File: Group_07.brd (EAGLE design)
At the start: 100 x 80 mm, 29 parts, among them J1 POWER_JACKPTH_LOCK, U1 +12v, U3 TCA9546ASO16, U4 TMUX1208

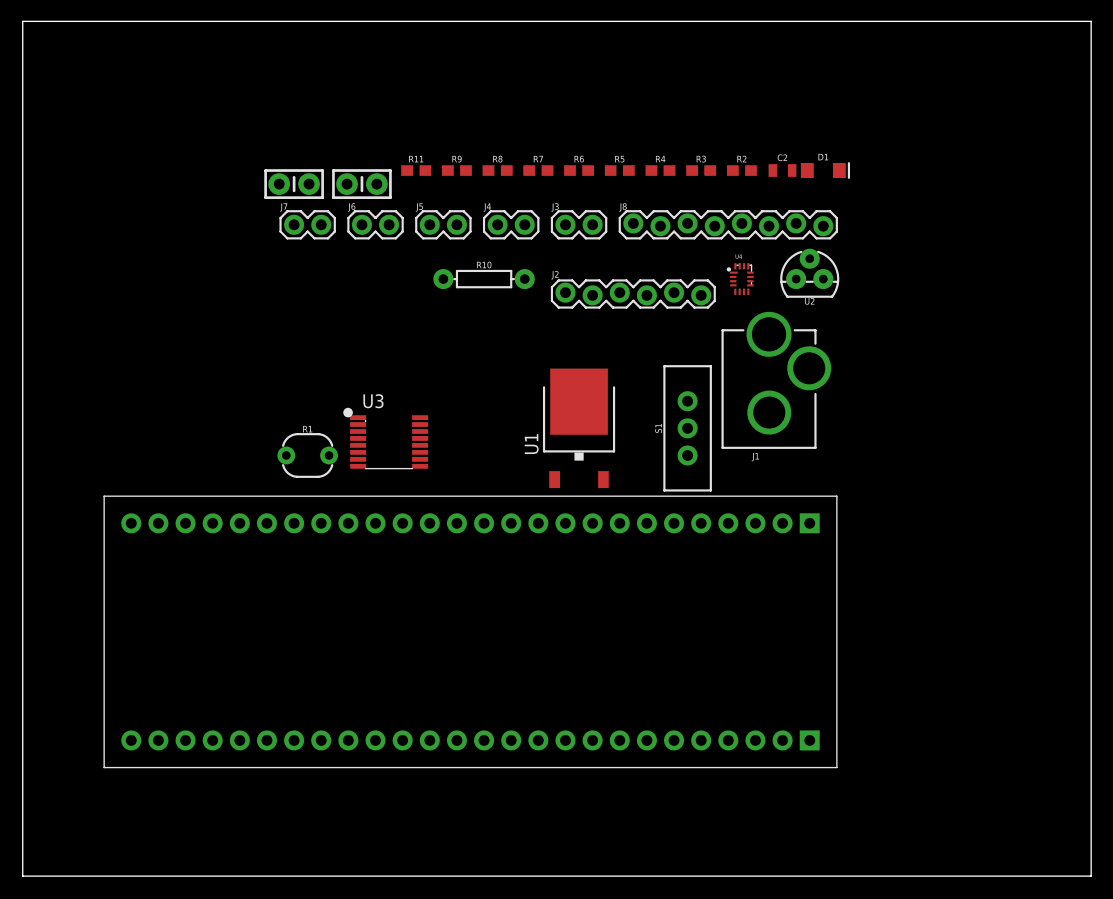
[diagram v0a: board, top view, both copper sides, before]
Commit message: Disposition of the components and traces
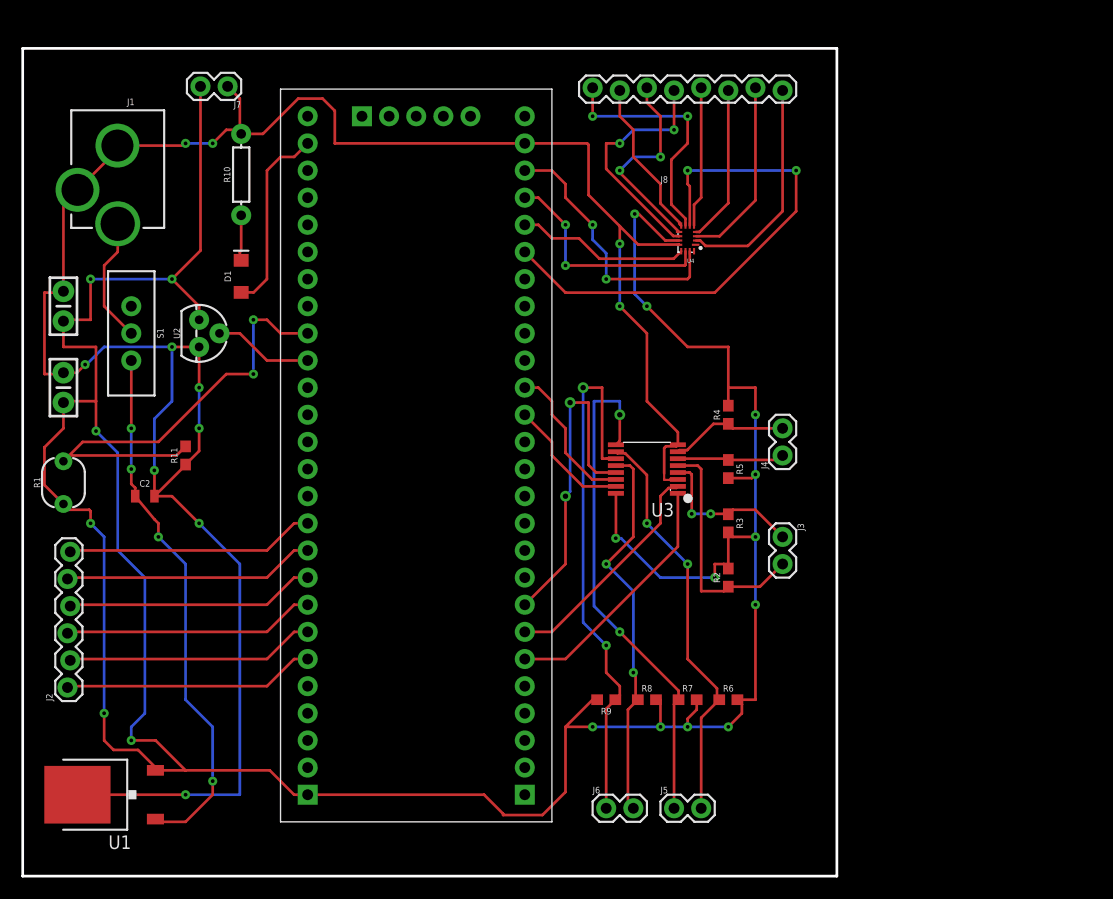
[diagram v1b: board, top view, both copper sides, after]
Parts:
- removed U$4: CY8CKIT-059_TARGET_3, CY8KIT-059:CY8CKIT-059_TARGET_3
- added U$1: CY8CKIT-059_TARGET, CYKIT:CY8CKIT-059_TARGET
- moved J1 71.9 mm to (8.89, 74.9), turned to 180 degrees
- moved C2 67.0 mm to (11.4, 35.6)
- moved J2 59.5 mm to (4.19, 17.7), turned to 90 degrees
- moved J5 59.2 mm to (61.0, 6.35)
- moved J6 59.2 mm to (54.6, 6.35)
- moved U2 57.4 mm to (16.5, 50.8), turned to 270 degrees
- moved U1 56.1 mm to (7.62, 7.62), turned to 90 degrees
- moved D1 55.4 mm to (20.4, 56.1), turned to 90 degrees
- moved S1 52.8 mm to (10.2, 50.8), turned to 180 degrees
- moved R6 51.5 mm to (66.0, 16.5)
- moved R7 51.5 mm to (62.2, 16.5)
- moved R8 51.5 mm to (58.4, 16.5)
- moved R9 51.5 mm to (54.6, 16.5), turned to 180 degrees
- moved R2 38.1 mm to (66.0, 27.9), turned to 90 degrees
- moved J3 35.6 mm to (71.1, 31.8), turned to 270 degrees
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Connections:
- removed net GND2: U$4.52
- net 5V: now also U$1.27; no longer U$4.27
- net GND: now also U$1.25; no longer U$4.25
- net I2C_A0: now also U$1.6; no longer U$4.6
- net I2C_A1: now also U$1.7; no longer U$4.7
- net I2C_A2: now also U$1.8; no longer U$4.8
- net I2C_SCL: now also U$1.16; no longer U$4.16
- net I2C_SDA: now also U$1.15; no longer U$4.15
- net MUX_A0/1.3C: now also U$1.24; no longer U$4.24
- net MUX_A1/1.4C: now also U$1.23; no longer U$4.23
- net MUX_A2/1.4C: now also U$1.22; no longer U$4.22
- net MUX_OUT/1.4C: now also U$1.21; no longer U$4.21
- net N$18: now also U$1.26; no longer U$4.26
- net N$20: now also U$1.28; no longer U$4.28
- net N$3: now also U$1.37; no longer U$4.37
- net N$4: now also U$1.36; no longer U$4.36
- net N$5: now also U$1.35; no longer U$4.35
- net N$6: now also U$1.34; no longer U$4.34
- net N$7: now also U$1.33; no longer U$4.33
- net N$8: now also U$1.32; no longer U$4.32
- net N$9: now also U$1.51; no longer U$4.51
- net PHOTO_OUT: now also U$1.44; no longer U$4.44
- net TEMP_OUT: now also U$1.43; no longer U$4.43
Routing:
- net 5V: track 0.00 -> 298.5 mm, vias 0 -> 18
- net GND: track 0.00 -> 216.8 mm, vias 0 -> 11
- net I2C_SDA_3: track 0.00 -> 51.9 mm, vias 0 -> 2
- net 12V: track 0.00 -> 50.2 mm, vias 0 -> 4
- net MUX_OUT/1.4C: track 0.00 -> 49.3 mm, vias 0 -> 2
- net I2C_SDA_2: track 0.00 -> 48.2 mm, vias 0 -> 2
- net PHOTO_OUT: track 0.00 -> 43.9 mm, vias 0 -> 2
- net I2C_SCL_2: track 0.00 -> 38.6 mm, vias 0 -> 2
- net I2C_SCL_3: track 0.00 -> 37.1 mm, vias 0 -> 2
- net I2C_A2: track 0.00 -> 31.1 mm, vias 0 -> 2
- net MUX_A0/1.3C: track 0.00 -> 25.1 mm, vias 0 -> 2
- net I2C_A0: track 0.00 -> 23.7 mm
- net N$8: track 0.00 -> 23.6 mm
- net N$4: track 0.00 -> 23.6 mm
- net N$6: track 0.00 -> 23.6 mm
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- added copper zone on layer 16, net 5V
- added copper zone on layer 1, net GND
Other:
- board size 100 x 80 mm -> 76.2 x 77.5 mm

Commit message: modifica delle dimensioni vias
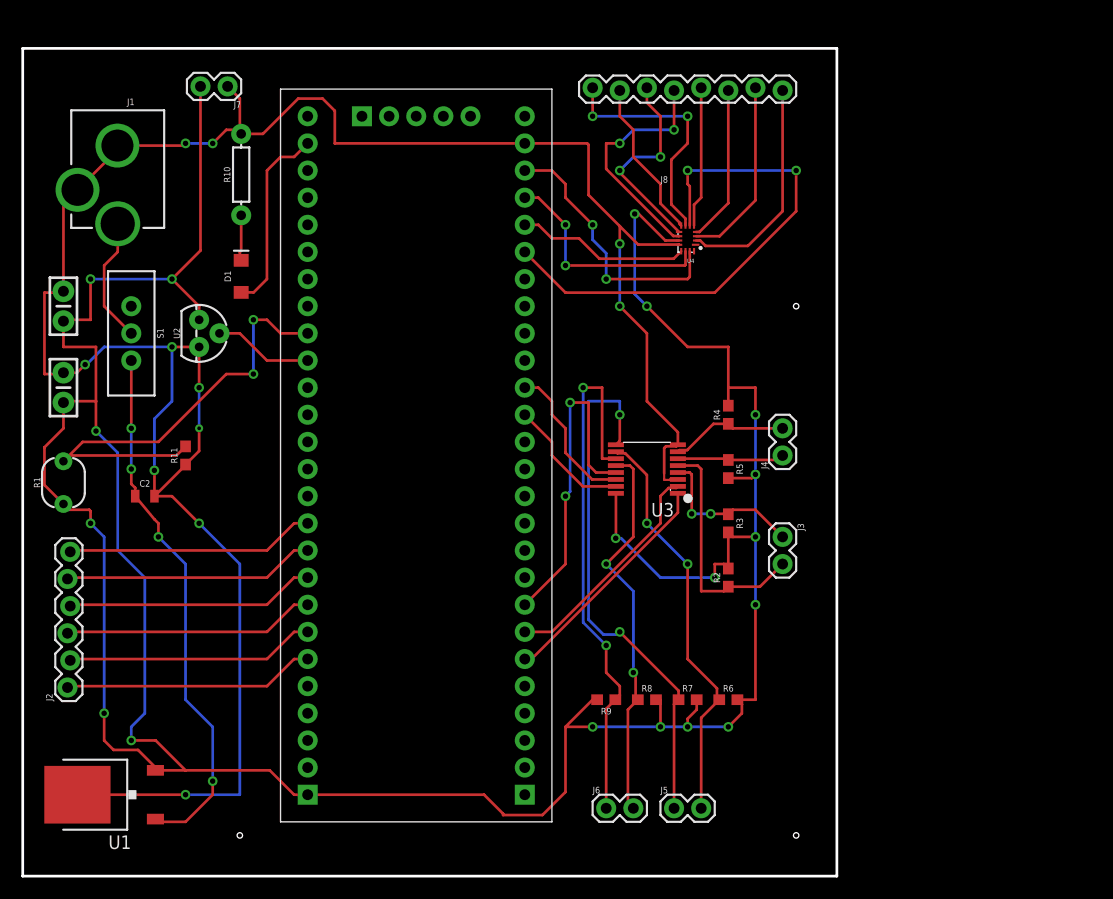
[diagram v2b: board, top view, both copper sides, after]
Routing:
- net I2C_SDA_2: track 48.2 -> 50.2 mm
- net I2C_A0: track 23.7 -> 21.8 mm
- net I2C_SDA_3: track 51.9 -> 51.0 mm

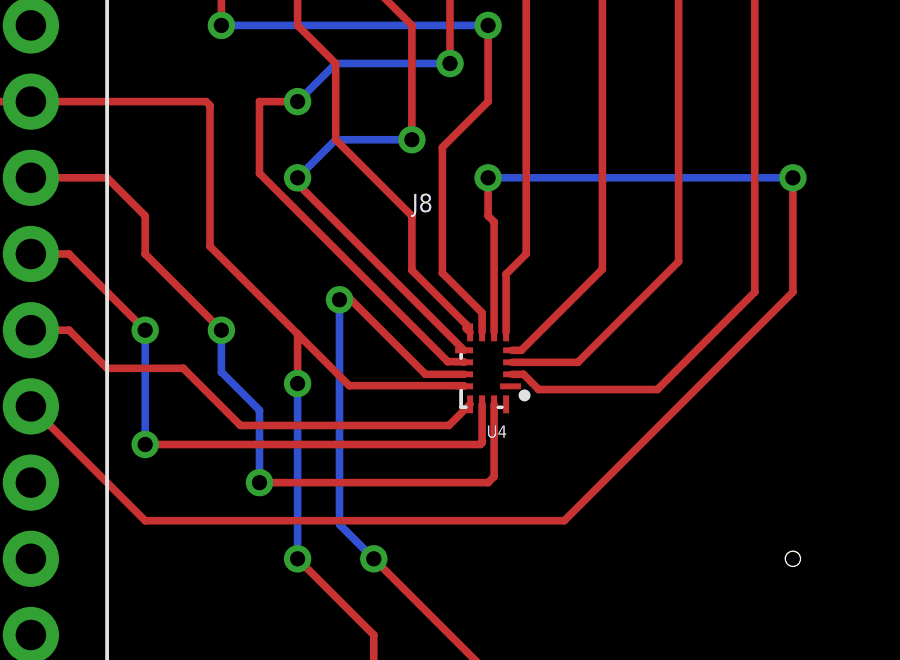
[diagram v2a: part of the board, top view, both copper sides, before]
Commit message: airwire da fixare per problemi di clearance
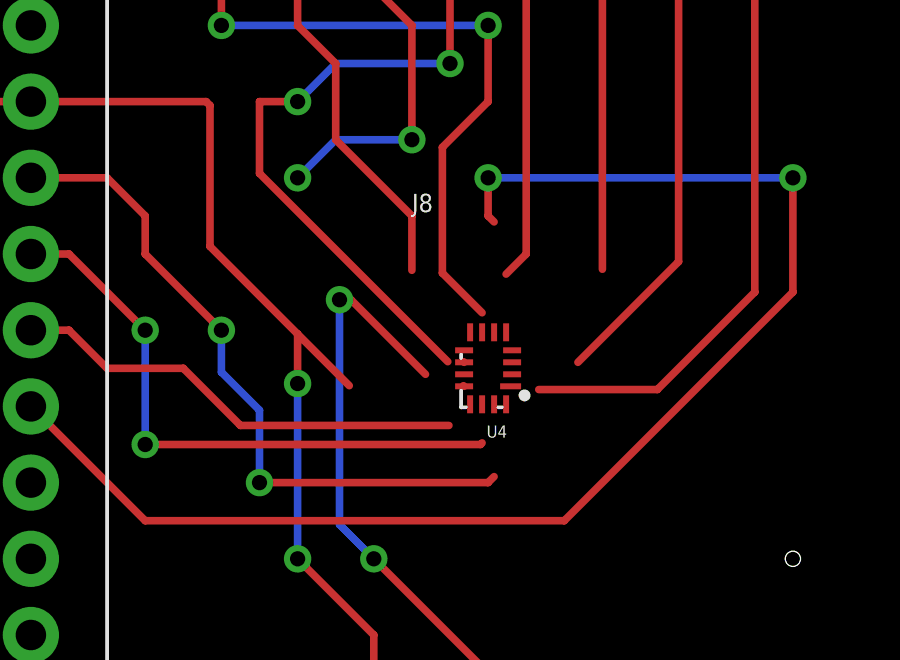
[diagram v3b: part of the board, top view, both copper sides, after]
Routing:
- net N$15: track 19.4 -> 11.5 mm
- net N$12: track 14.7 -> 10.5 mm
- net GND: track 216.7 -> 212.9 mm
- net MUX_OUT/1.4C: track 49.3 -> 45.7 mm
- net N$16: track 15.0 -> 12.2 mm
- net MUX_A0/1.3C: track 25.1 -> 22.7 mm
- net N$11: track 17.5 -> 15.3 mm
- net N$13: track 13.2 -> 11.2 mm
- net MUX_A1/1.4C: track 21.2 -> 19.9 mm
- net 5V: track 298.5 -> 297.2 mm
- net N$2: track 20.9 -> 19.8 mm
- net MUX_A2/1.4C: track 16.2 -> 15.3 mm
- net N$17: track 23.0 -> 22.3 mm
- net N$14: track 22.4 -> 21.9 mm
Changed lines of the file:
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@@
 <wire x1="2.032" y1="40.132" x2="2.032" y2="36.608" width="0.254" layer="1"/>
 <wire x1="2.032" y1="36.608" x2="3.81" y2="34.83" width="0.254" layer="1"/>
-<wire x1="61.43" y1="59.49" x2="60.144" y2="59.49" width="0.254" layer="1"/>
 <wire x1="57.658" y1="61.976" x2="57.277" y2="61.976" width="0.254" layer="1"/>
 <via x="57.277" y="61.976" extent="1-16" drill="0.508"/>
@@
 <wire x1="7.62" y1="31.75" x2="7.62" y2="15.24" width="0.254" layer="16"/>
 <wire x1="8.509" y1="11.811" x2="10.789" y2="11.811" width="0.254" layer="1"/>
+<wire x1="60.144" y1="59.49" x2="61.43" y2="59.49" width="0" layer="19" extent="1-1"/>
 </signal>
 <signal name="N$1">
@@
 </polygon>
 <wire x1="61.43" y1="59.09" x2="61.4094" y2="59.1106" width="0.254" layer="1"/>
-<wire x1="61.4094" y1="59.1106" x2="57.6024" y2="59.1106" width="0.254" layer="1"/>
 <wire x1="57.6024" y1="59.1106" x2="55.88" y2="60.833" width="0.254" layer="1"/>
 <wire x1="55.88" y1="60.833" x2="52.959" y2="63.754" width="0.254" layer="1"/>
@@
 <wire x1="60.071" y1="37.084" x2="60.5552" y2="37.084" width="0.2032" layer="1"/>
 <wire x1="60.5552" y1="37.084" x2="60.5962" y2="37.125" width="0.2032" layer="1"/>
+<wire x1="57.6024" y1="59.1106" x2="61.4094" y2="59.1106" width="0" layer="19" extent="1-1"/>
 </signal>
 <signal name="12V">
@@
 <contactref element="U$1" pad="24"/>
 <contactref element="U4" pad="15"/>
-<wire x1="62.43" y1="58.49" x2="62.43" y2="56.08" width="0.254" layer="1"/>
 <wire x1="62.43" y1="56.08" x2="62.23" y2="55.88" width="0.254" layer="1"/>
 <wire x1="62.23" y1="55.88" x2="54.61" y2="55.88" width="0.254" layer="1"/>
@@
 <wire x1="50.8" y1="64.77" x2="49.53" y2="66.04" width="0.254" layer="1"/>
 <wire x1="49.53" y1="66.04" x2="46.99" y2="66.04" width="0.254" layer="1"/>
+<wire x1="62.43" y1="56.08" x2="62.43" y2="58.49" width="0" layer="19" extent="1-1"/>
 </signal>
 <signal name="MUX_A1/1.4C">
 <contactref element="U$1" pad="23"/>
 <contactref element="U4" pad="14"/>
-<wire x1="62.03" y1="58.49" x2="62.03" y2="57.204" width="0.254" layer="1"/>
 <wire x1="62.03" y1="57.204" x2="61.976" y2="57.15" width="0.254" layer="1"/>
 <wire x1="61.976" y1="57.15" x2="50.8" y2="57.15" width="0.254" layer="1"/>
@@
 <wire x1="50.8" y1="60.96" x2="48.26" y2="63.5" width="0.254" layer="1"/>
 <wire x1="48.26" y1="63.5" x2="46.99" y2="63.5" width="0.254" layer="1"/>
+<wire x1="62.03" y1="57.204" x2="62.03" y2="58.49" width="0" layer="19" extent="1-1"/>
 </signal>
 <signal name="MUX_A2/1.4C">
@@
 <wire x1="52.07" y1="59.69" x2="53.975" y2="57.785" width="0.254" layer="1"/>
 <wire x1="53.975" y1="57.785" x2="60.925" y2="57.785" width="0.254" layer="1"/>
-<wire x1="60.925" y1="57.785" x2="61.63" y2="58.49" width="0.254" layer="1"/>
+<wire x1="60.925" y1="57.785" x2="61.63" y2="58.49" width="0" layer="19" extent="1-1"/>
 </signal>
 <signal name="MUX_OUT/1.4C">
 <contactref element="U$1" pad="21"/>
 <contactref element="U4" pad="6"/>
-<wire x1="62.43" y1="60.89" x2="62.43" y2="64.57" width="0.254" layer="1"/>
 <wire x1="62.43" y1="64.57" x2="62.23" y2="64.77" width="0.254" layer="1"/>
 <wire x1="62.23" y1="64.77" x2="62.23" y2="66.04" width="0.254" layer="1"/>
@@
 <wire x1="64.77" y1="54.61" x2="50.8" y2="54.61" width="0.254" layer="1"/>
 <wire x1="50.8" y1="54.61" x2="46.99" y2="58.42" width="0.254" layer="1"/>
+<wire x1="62.43" y1="64.57" x2="62.43" y2="60.89" width="0" layer="19" extent="1-1"/>
 </signal>
 <signal name="N$2">
@@
 <contactref element="U4" pad="2"/>
 <wire x1="67.872" y1="58.982" x2="63.919" y2="58.982" width="0.254" layer="1"/>
-<wire x1="63.919" y1="58.982" x2="63.411" y2="59.49" width="0.254" layer="1"/>
-<wire x1="63.03" y1="59.49" x2="63.411" y2="59.49" width="0.254" layer="1"/>
 <wire x1="67.872" y1="58.982" x2="71.12" y2="62.23" width="0.254" layer="1"/>
 <wire x1="71.12" y1="62.23" x2="71.12" y2="73.533" width="0.254" layer="1"/>
+<wire x1="63.03" y1="59.49" x2="63.919" y2="58.982" width="0" layer="19" extent="1-1"/>
 </signal>
 <signal name="N$11">
 <contactref element="J8" pad="7"/>
 <contactref element="U4" pad="3"/>
-<wire x1="63.03" y1="59.89" x2="65.224" y2="59.89" width="0.254" layer="1"/>
 <wire x1="65.224" y1="59.89" x2="68.58" y2="63.246" width="0.254" layer="1"/>
 <wire x1="68.58" y1="63.246" x2="68.58" y2="73.787" width="0.254" layer="1"/>
+<wire x1="63.03" y1="59.89" x2="65.224" y2="59.89" width="0" layer="19" extent="1-1"/>
 </signal>
 <signal name="N$12">
 <contactref element="J8" pad="6"/>
 <contactref element="U4" pad="4"/>
-<wire x1="63.03" y1="60.29" x2="63.338" y2="60.29" width="0.254" layer="1"/>
 <wire x1="66.04" y1="62.992" x2="66.04" y2="73.533" width="0.254" layer="1"/>
-<wire x1="63.338" y1="60.29" x2="66.04" y2="62.992" width="0.254" layer="1"/>
+<wire x1="63.03" y1="60.29" x2="66.04" y2="62.992" width="0" layer="19" extent="1-1"/>
 </signal>
 <signal name="N$13">
 <contactref element="J8" pad="5"/>
 <contactref element="U4" pad="5"/>
-<wire x1="62.83" y1="60.89" x2="62.83" y2="62.83" width="0.254" layer="1"/>
-<wire x1="62.83" y1="62.83" x2="63.5" y2="63.5" width="0.254" layer="1"/>
+<wire x1="63.5" y1="63.5" x2="62.83" y2="62.83" width="0.254" layer="1"/>
 <wire x1="63.5" y1="63.5" x2="63.5" y2="73.787" width="0.254" layer="1"/>
+<wire x1="62.83" y1="62.83" x2="62.83" y2="60.89" width="0" layer="19" extent="1-1"/>
 </signal>
 <signal name="N$14">
@@
 <contactref element="U4" pad="10"/>
 <wire x1="61.43" y1="59.89" x2="61.4094" y2="59.9106" width="0.254" layer="1"/>
-<wire x1="61.4094" y1="59.9106" x2="60.88726875" y2="59.9106" width="0.254" layer="1"/>
 <wire x1="60.88726875" y1="59.9106" x2="54.61" y2="66.18786875" width="0.254" layer="1"/>
 <wire x1="54.61" y1="66.18786875" x2="54.61" y2="68.58" width="0.254" layer="1"/>
@@
 <wire x1="60.96" y1="69.85" x2="60.96" y2="73.533" width="0.254" layer="1"/>
 <wire x1="57.15" y1="69.85" x2="60.96" y2="69.85" width="0.254" layer="16"/>
+<wire x1="60.88726875" y1="59.9106" x2="61.4094" y2="59.9106" width="0" layer="19" extent="1-1"/>
 </signal>
 <signal name="N$15">
@@
 <wire x1="59.69" y1="71.12" x2="58.42" y2="72.39" width="0.254" layer="1"/>
 <wire x1="58.42" y1="72.39" x2="58.42" y2="73.787" width="0.254" layer="1"/>
-<wire x1="61.43" y1="60.29" x2="55.88" y2="65.84" width="0.254" layer="1"/>
 <wire x1="55.88" y1="65.84" x2="55.88" y2="66.04" width="0.254" layer="1"/>
 <via x="55.88" y="66.04" extent="1-16" drill="0.508"/>
@@
 <via x="59.69" y="67.31" extent="1-16" drill="0.508"/>
 <wire x1="59.69" y1="67.31" x2="59.69" y2="71.12" width="0.254" layer="1"/>
+<wire x1="59.69" y1="67.31" x2="61.43" y2="60.29" width="0" layer="19" extent="1-1"/>
 </signal>
 <signal name="N$16">
 <contactref element="J8" pad="2"/>
 <contactref element="U4" pad="8"/>
-<wire x1="61.503" y1="61.144" x2="61.503" y2="61.017" width="0.254" layer="1"/>
-<wire x1="61.63" y1="60.89" x2="61.503" y2="61.017" width="0.254" layer="1"/>
-<wire x1="61.503" y1="61.144" x2="59.69" y2="62.957" width="0.254" layer="1"/>
 <wire x1="59.69" y1="62.957" x2="59.69" y2="64.77" width="0.254" layer="1"/>
 <wire x1="57.15" y1="69.85" x2="55.88" y2="71.12" width="0.254" layer="1"/>
@@
 <wire x1="59.69" y1="64.77" x2="57.15" y2="67.31" width="0.254" layer="1"/>
 <wire x1="57.15" y1="67.31" x2="57.15" y2="69.85" width="0.254" layer="1"/>
+<wire x1="59.69" y1="62.957" x2="61.63" y2="60.89" width="0" layer="19" extent="1-1"/>
 </signal>
 <signal name="N$17">
@@
 <via x="53.34" y="71.12" extent="1-16" drill="0.508"/>
 <wire x1="53.34" y1="71.12" x2="53.34" y2="73.787" width="0.254" layer="1"/>
-<wire x1="62.03" y1="60.89" x2="62.03" y2="61.541" width="0.254" layer="1"/>
-<wire x1="62.03" y1="61.541" x2="60.706" y2="62.865" width="0.254" layer="1"/>
+<wire x1="60.706" y1="62.865" x2="62.03" y2="61.541" width="0.254" layer="1"/>
 <wire x1="60.706" y1="62.865" x2="60.706" y2="67.056" width="0.254" layer="1"/>
 <wire x1="60.706" y1="67.056" x2="62.23" y2="68.58" width="0.254" layer="1"/>
+<wire x1="62.03" y1="61.541" x2="62.03" y2="60.89" width="0" layer="19" extent="1-1"/>
 </signal>
 <signal name="N$19">
